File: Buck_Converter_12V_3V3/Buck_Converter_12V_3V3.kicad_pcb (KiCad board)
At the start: 2 copper layers, 138 x 88.5 mm, 14 parts

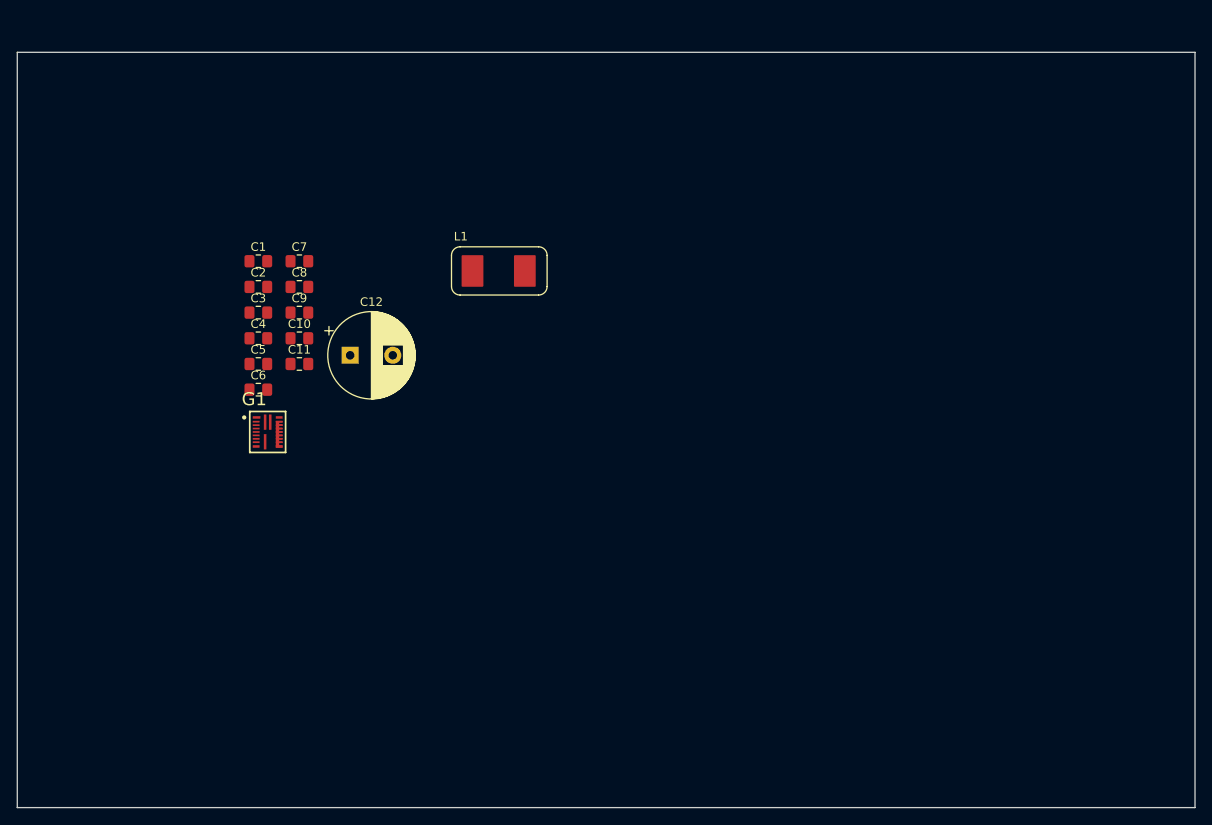
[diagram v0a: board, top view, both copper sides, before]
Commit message: Layout Complete
Vis Stiching pending.
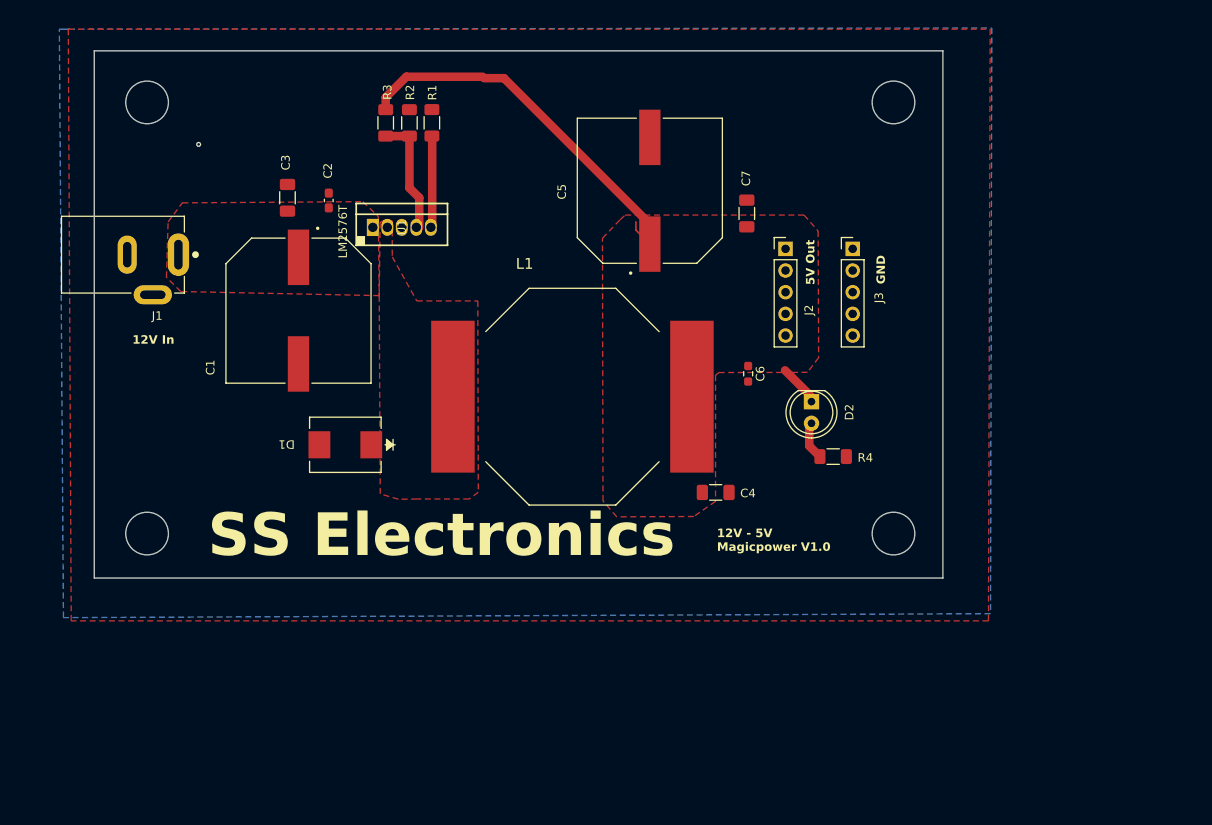
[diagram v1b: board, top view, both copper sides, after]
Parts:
- removed C10, C11, C8, C9: 22uF, Capacitor_SMD:C_0805_2012Metric_Pad1.18x1.45mm_HandSolder
- removed C12: 330uF, Capacitor_THT:CP_Radial_D10.0mm_P5.00mm
- removed G1: TDA38813, TDA38813:IFX-PG-QFN-21-V
- added D1: D_Schottky, Diodes:SMC_DIO-M, F.Cu at (101.4, 97.5)
- added D2: LED, LED_THT:LED_D5.0mm, F.Cu at (156.1, 92.4)
- added J1: PJ-002B, Connector:CUI_PJ-002B, F.Cu at (81.9, 75.2)
- added J2: 5V @ 3A, Connector_PinHeader_2.54mm:PinHeader_1x05_P2.54mm_Vertical, F.Cu at (153.0, 74.5)
- added J3: GND, Connector_PinHeader_2.54mm:PinHeader_1x05_P2.54mm_Vertical, F.Cu at (160.9, 74.5)
- added R1: 1.02k, Resistor_SMD:R_1206_3216Metric_Pad1.30x1.75mm_HandSolder, F.Cu at (111.6, 59.8)
- added R2: 3.01K, Resistor_SMD:R_1206_3216Metric_Pad1.30x1.75mm_HandSolder, F.Cu at (106.2, 59.8)
- added R3: 1K, Resistor_SMD:R_1206_3216Metric_Pad1.30x1.75mm_HandSolder, F.Cu at (109.0, 59.8)
- added R4: 100E, Resistor_SMD:R_1206_3216Metric_Pad1.30x1.75mm_HandSolder, F.Cu at (158.6, 98.9)
- added U1: LM2576T, LM2576:LM2576xx, F.Cu at (108.1, 72.0)
- C1: value 22uF -> 470uF; footprint Capacitor_SMD:C_0805_2012Metric_Pad1.18x1.45mm_HandSolder -> Capacitor:CAP_EEVFK1J471M
- C2: value 22uF -> 0.022uF; footprint Capacitor_SMD:C_0805_2012Metric_Pad1.18x1.45mm_HandSolder -> Capacitor_SMD:C_0603_1608Metric_Pad1.08x0.95mm_HandSolder
- C3, C4, C7: value 22uF -> 0.47uF; footprint Capacitor_SMD:C_0805_2012Metric_Pad1.18x1.45mm_HandSolder -> Capacitor_SMD:C_1206_3216Metric_Pad1.33x1.80mm_HandSolder
- C5: value 22uF -> 2200uF; footprint Capacitor_SMD:C_0805_2012Metric_Pad1.18x1.45mm_HandSolder -> Capacitor:CAP_EEVFK1E222M
- C6: value 22uF -> 0.22uF; footprint Capacitor_SMD:C_0805_2012Metric_Pad1.18x1.45mm_HandSolder -> Resistor_SMD:R_0603_1608Metric_Pad0.98x0.95mm_HandSolder
- L1: value 240nH -> PM2120-101K-RC; footprint Choke_Coil:Choke_Coil_SMD_3.5_8.4 -> Inductor:PM2120271KRC
- moved C6 57.4 mm to (148.6, 89.2), turned to -90 degrees
- moved C4 56.6 mm to (144.8, 103.1)
- moved C7 52.7 mm to (148.5, 70.4), turned to 90 degrees
- moved C5 50.2 mm to (137.1, 67.7), turned to 90 degrees
- moved L1 17.1 mm to (128.1, 91.8)
- moved C3 13.9 mm to (94.7, 68.5), turned to 90 degrees
- moved C2 13.1 mm to (99.5, 68.9), turned to 90 degrees
- moved C1 7.46 mm to (96.0, 81.8), turned to -90 degrees
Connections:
- C1 pad 1: 12V_IN -> Net-(U1-VIN)
- C2 pad 1: 12V_IN -> Net-(U1-VIN)
- C3 pad 1: 12V_IN -> Net-(U1-VIN)
- C4 pad 1: 12V_IN -> Net-(D2-K)
- C5 pad 1: 12V_IN -> Net-(D2-K)
- C6 pad 1: 12V_IN -> Net-(D2-K)
- C7 pad 1: 12V_IN -> Net-(D2-K)
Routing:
- net Net-(D2-K): track 0.00 -> 50.6 mm
- net Net-(U1-FB): track 0.00 -> 13.9 mm
- net Net-(U1-ON_OFF_N): track 0.00 -> 10.9 mm
- net Net-(D2-A): track 0.00 -> 4.64 mm
- net GND: vias 0 -> 1
- added copper zone on B.Cu, net GND
- added copper zone on F.Cu, net GND
- added copper zone on F.Cu, net Net-(D1-K)
- added copper zone on F.Cu, net Net-(D2-K)
- added copper zone on F.Cu, net Net-(U1-VIN)
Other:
- board size 138 x 88.5 mm -> 99.4 x 61.8 mm
- board text added: "12V - 5V Magicpower V1.0"
- board text added: "12V In"
- board text added: "5V Out"
- board text added: "GND"
- board text added: "SS Electronics"

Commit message: :rocket: Magicpower V1.0.0 Release
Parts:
- removed D2: LED, LED_THT:LED_D5.0mm
- removed R2: 3.01K, Resistor_SMD:R_1206_3216Metric_Pad1.30x1.75mm_HandSolder
- removed R3: 1K, Resistor_SMD:R_1206_3216Metric_Pad1.30x1.75mm_HandSolder
- removed R4: 100E, Resistor_SMD:R_1206_3216Metric_Pad1.30x1.75mm_HandSolder
- added RV1: R_Potentiometer, SS_Resistors:601030_AVX, F.Cu at (102.0, 57.0)
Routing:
- net Net-(D2-A): track 4.64 -> 0.00 mm
- net Net-(J2-Pin_1): track 50.6 -> 48.9 mm
- net GND: vias 1 -> 359
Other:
- outline, holes or cut-outs redrawn
- board text added: "7V - 40V In"
- board text added: "Magic Power V1.0"
- board text added: "Vin : 7 -40 V Iout: 3A"
- board text added: "Vout Adj"
- board text added: "Vout value: Check manually"
- board text added: "Vout: Adj Iout: 3A Max"
- board text removed: "12V - 5V Magicpower V1.0"
- board text removed: "12V In"
